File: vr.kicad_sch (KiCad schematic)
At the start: 28 parts, among them U2 ST1PS02CQTR, U3 ST1PS02CQTR, U303 LDLN025M12R, U304 LM2664M6_NOPB

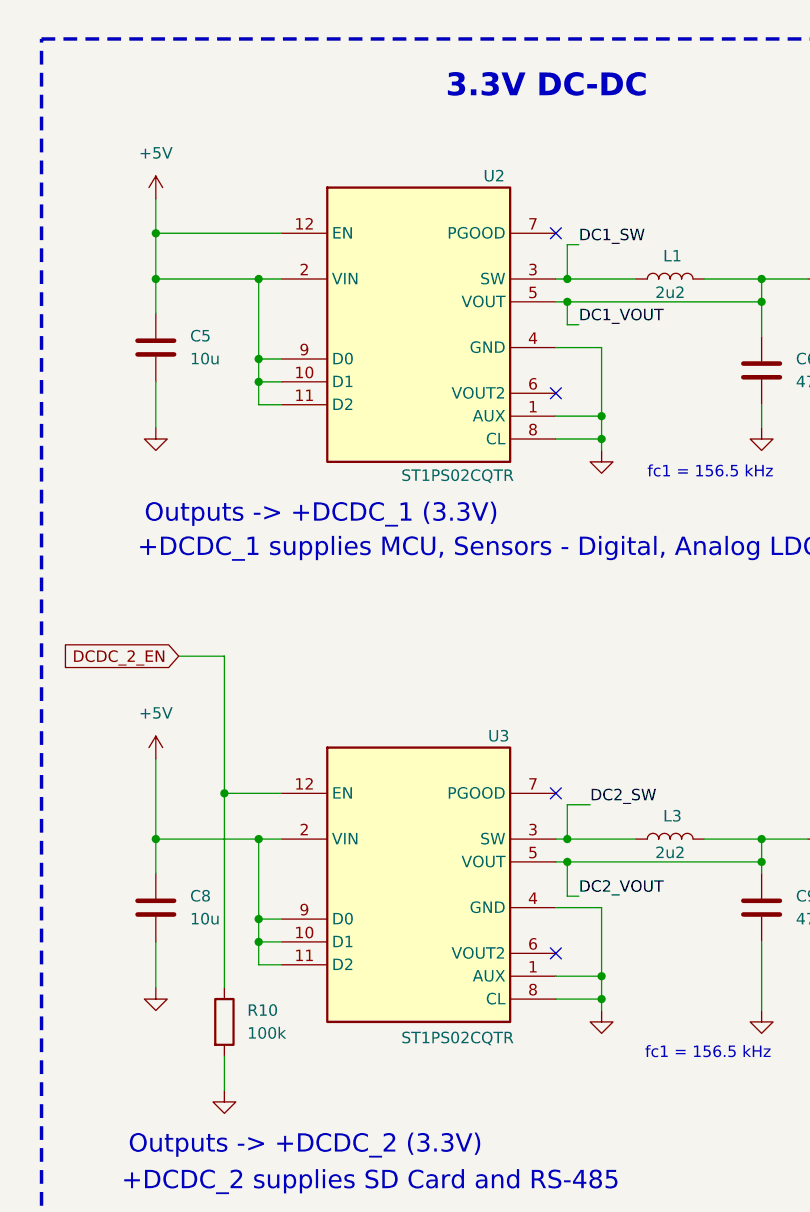
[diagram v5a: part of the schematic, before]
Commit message: schematics errors fixed and ready for PCB
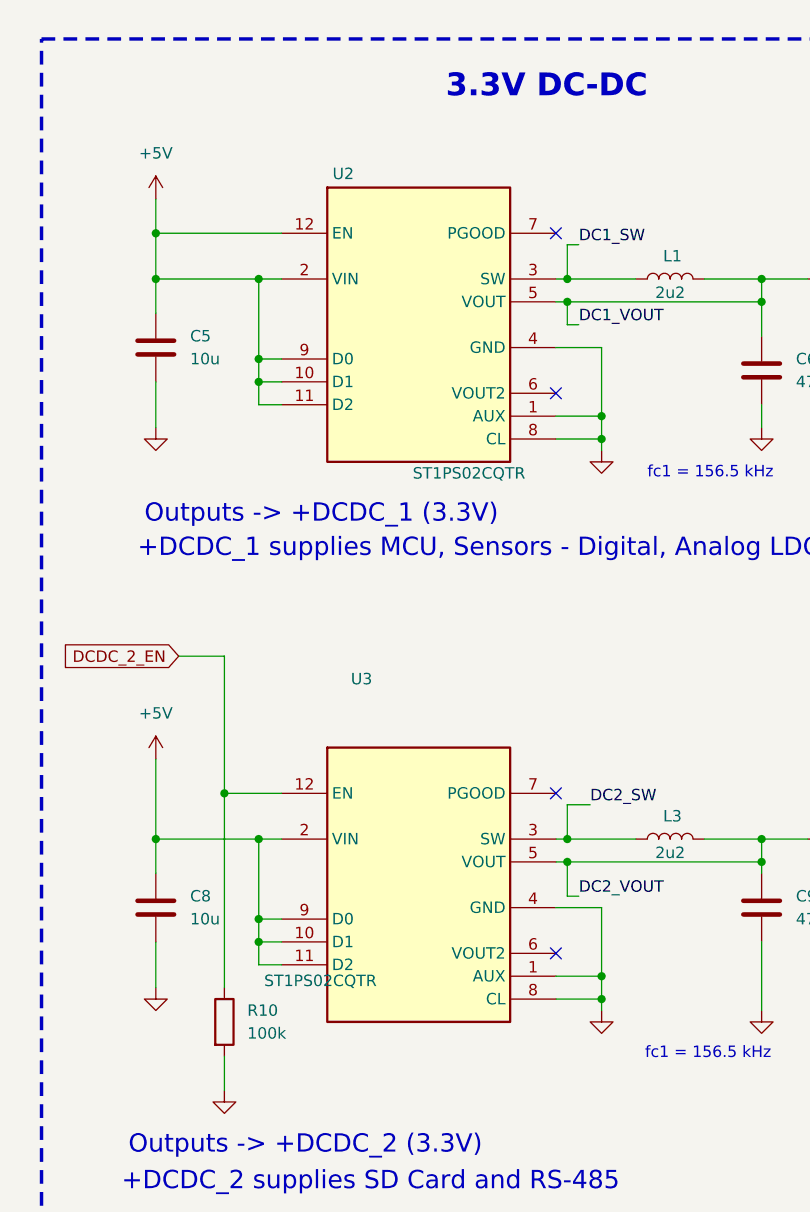
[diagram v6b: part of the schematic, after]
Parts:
- TP2, TP3, TP302, TP304: Distributor_Link https://www.mouser.com/ProductDetail/Keystone-Electronics/5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 -> (none); Manufacturer_Name Keystone Electronics -> (none); Manufacturer_Part_Number 5000 -> (none)
- U2, U3: footprint EMS:ST1PS02CQTR -> QFN40P170X200X55-12N-D; symbol AMS-CM:ST1PS02CQTR -> EMS:ST1PS02CQTR
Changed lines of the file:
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@@
 			)
 		)
-		(property "Datasheet" "https://www.mouser.com/datasheet/2/215/000-5004-741320.pdf"
+		(property "Datasheet" "~"
 			(at 80.01 189.23 0)
 			(effects
@@
 			)
 		)
-		(property "Distributor_Link" "https://www.mouser.com/ProductDetail/Keystone-Electronics/5000?qs=q0tsjPZWdm%252B9SiiTAbEwUw%3D%3D"
+		(property "Distributor_Link" "~"
 			(at 80.01 194.31 0)
 			(effects
@@
 			)
 		)
-		(property "Manufacturer_Name" "Keystone Electronics"
+		(property "Manufacturer_Name" "~"
 			(at 80.01 194.31 0)
 			(effects
@@
 			)
 		)
-		(property "Manufacturer_Part_Number" "5000"
+		(property "Manufacturer_Part_Number" "~"
 			(at 80.01 194.31 0)
 			(effects
@@
 			)
 		)
-		(property "Datasheet" "https://www.mouser.com/datasheet/2/215/000-5004-741320.pdf"
+		(property "Datasheet" "~"
 			(at 43.18 189.23 0)
 			(effects
@@
 			)
 		)
-		(property "Distributor_Link" "https://www.mouser.com/ProductDetail/Keystone-Electronics/5000?qs=q0tsjPZWdm%252B9SiiTAbEwUw%3D%3D"
+		(property "Distributor_Link" "~"
 			(at 43.18 194.31 0)
 			(effects
@@
 			)
 		)
-		(property "Manufacturer_Name" "Keystone Electronics"
+		(property "Manufacturer_Name" "~"
 			(at 43.18 194.31 0)
 			(effects
@@
 			)
 		)
-		(property "Manufacturer_Part_Number" "5000"
+		(property "Manufacturer_Part_Number" "~"
 			(at 43.18 194.31 0)
 			(effects
@@
 			)
 		)
-		(property "Datasheet" "https://www.mouser.com/datasheet/2/215/000-5004-741320.pdf"
+		(property "Datasheet" "~"
 			(at 62.23 189.23 0)
 			(effects
@@
 			)
 		)
-		(property "Distributor_Link" "https://www.mouser.com/ProductDetail/Keystone-Electronics/5000?qs=q0tsjPZWdm%252B9SiiTAbEwUw%3D%3D"
+		(property "Distributor_Link" "~"
 			(at 62.23 194.31 0)
 			(effects
@@
 			)
 		)
-		(property "Manufacturer_Name" "Keystone Electronics"
+		(property "Manufacturer_Name" "~"
 			(at 62.23 194.31 0)
 			(effects
@@
 			)
 		)
-		(property "Manufacturer_Part_Number" "5000"
+		(property "Manufacturer_Part_Number" "~"
 			(at 62.23 194.31 0)
 			(effects
@@
 			)
 		)
-		(property "Datasheet" "https://www.mouser.com/datasheet/2/215/000-5004-741320.pdf"
+		(property "Datasheet" "~"
 			(at 24.13 189.23 0)
 			(effects
@@
 			)
 		)
-		(property "Distributor_Link" "https://www.mouser.com/ProductDetail/Keystone-Electronics/5000?qs=q0tsjPZWdm%252B9SiiTAbEwUw%3D%3D"
+		(property "Distributor_Link" "~"
 			(at 24.13 194.31 0)
 			(effects
@@
 			)
 		)
-		(property "Manufacturer_Name" "Keystone Electronics"
+		(property "Manufacturer_Name" "~"
 			(at 24.13 194.31 0)
 			(effects
@@
 			)
 		)
-		(property "Manufacturer_Part_Number" "5000"
+		(property "Manufacturer_Part_Number" "~"
 			(at 24.13 194.31 0)
 			(effects
@@
 	)
 	(symbol
-		(lib_id "AMS-CM:ST1PS02CQTR")
-		(at 57.15 123.19 0)
+		(lib_id "EMS:ST1PS02CQTR")
+		(at 41.91 116.84 0)
 		(unit 1)
 		(exclude_from_sim no)
@@
 		(dnp no)
 		(property "Reference" "U3"
-			(at 66.04 107.95 0)
+			(at 50.8 101.6 0)
 			(effects
 				(font
@@
 		)
 		(property "Value" "ST1PS02CQTR"
-			(at 61.468 141.478 0)
+			(at 46.228 135.128 0)
 			(effects
 				(font
@@
 			)
 		)
-		(property "Footprint" "EMS:ST1PS02CQTR"
+		(property "Footprint" "QFN40P170X200X55-12N-D"
 			(at 43.434 148.59 0)
 			(effects
@@
 		)
 		(property "Height" "0.55"
-			(at 83.82 513.03 0)
+			(at 68.58 506.68 0)
 			(effects
 				(font
@@
 		)
 		(property "Mouser Part Number" "511-ST1PS02CQTR"
-			(at 83.82 613.03 0)
+			(at 68.58 606.68 0)
 			(effects
 				(font
@@
 		)
 		(property "Mouser Price/Stock" "https://www.mouser.co.uk/ProductDetail/STMicroelectronics/ST1PS02CQTR?qs=sPbYRqrBIVkrGj42PMRzhg%3D%3D"
-			(at 83.82 713.03 0)
+			(at 68.58 706.68 0)
 			(effects
 				(font
@@
 		)
 		(property "Manufacturer_Name" "STMicroelectronics"
-			(at 83.82 813.03 0)
+			(at 68.58 806.68 0)
 			(effects
 				(font
@@
 		)
 		(property "Manufacturer_Part_Number" "ST1PS02CQTR"
-			(at 83.82 913.03 0)
+			(at 68.58 906.68 0)
 			(effects
 				(font
@@
 		)
 		(property "Arrow Part Number" ""
-			(at 57.15 123.19 0)
+			(at 41.91 116.84 0)
 			(effects
 				(font
@@
 		)
 		(property "Arrow Price/Stock" ""
-			(at 57.15 123.19 0)
+			(at 41.91 116.84 0)
 			(effects
 				(font
@@
 		)
 		(property "Distributor_Link" "https://www.mouser.co.uk/ProductDetail/STMicroelectronics/ST1PS02CQTR?qs=sPbYRqrBIVkrGj42PMRzhg%3D%3D"
-			(at 57.15 123.19 0)
+			(at 41.91 116.84 0)
 			(effects
 				(font
@@
 	)
 	(symbol
-		(lib_id "AMS-CM:ST1PS02CQTR")
-		(at 57.15 60.96 0)
+		(lib_id "EMS:ST1PS02CQTR")
+		(at 41.91 54.61 0)
 		(unit 1)
 		(exclude_from_sim no)
@@
 		(dnp no)
 		(property "Reference" "U2"
-			(at 65.532 45.72 0)
+			(at 48.768 45.466 0)
 			(effects
 				(font
@@
 		)
 		(property "Value" "ST1PS02CQTR"
-			(at 61.468 78.994 0)
+			(at 62.738 78.74 0)
 			(effects
 				(font
@@
 			)
 		)
-		(property "Footprint" "EMS:ST1PS02CQTR"
+		(property "Footprint" "QFN40P170X200X55-12N-D"
 			(at 43.434 86.36 0)
 			(effects
@@
 		)
 		(property "Height" "0.55"
-			(at 83.82 450.8 0)
+			(at 68.58 444.45 0)
 			(effects
 				(font
@@
 		)
 		(property "Mouser Part Number" "511-ST1PS02CQTR"
-			(at 83.82 550.8 0)
+			(at 68.58 544.45 0)
 			(effects
 				(font
@@
 		)
 		(property "Mouser Price/Stock" "https://www.mouser.co.uk/ProductDetail/STMicroelectronics/ST1PS02CQTR?qs=sPbYRqrBIVkrGj42PMRzhg%3D%3D"
-			(at 83.82 650.8 0)
+			(at 68.58 644.45 0)
 			(effects
 				(font
@@
 		)
 		(property "Manufacturer_Name" "STMicroelectronics"
-			(at 83.82 750.8 0)
+			(at 68.58 744.45 0)
 			(effects
 				(font
@@
 		)
 		(property "Manufacturer_Part_Number" "ST1PS02CQTR"
-			(at 83.82 850.8 0)
+			(at 68.58 844.45 0)
 			(effects
 				(font
@@
 		)
 		(property "Arrow Part Number" ""
-			(at 57.15 60.96 0)
+			(at 41.91 54.61 0)
 			(effects
 				(font
@@
 		)
 		(property "Arrow Price/Stock" ""
-			(at 57.15 60.96 0)
+			(at 41.91 54.61 0)
 			(effects
 				(font
@@
 		)
 		(property "Distributor_Link" "https://www.mouser.co.uk/ProductDetail/STMicroelectronics/ST1PS02CQTR?qs=sPbYRqrBIVkrGj42PMRzhg%3D%3D"
-			(at 57.15 60.96 0)
+			(at 41.91 54.61 0)
 			(effects
 				(font

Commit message: new version created. Now at v2.0.0
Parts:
- U2, U3: footprint QFN40P170X200X55-12N-D -> EMS:ST1PS02CQTR
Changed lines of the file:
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@@
 			)
 		)
-		(property "Footprint" "QFN40P170X200X55-12N-D"
+		(property "Footprint" "EMS:ST1PS02CQTR"
 			(at 43.434 148.59 0)
 			(effects
@@
 			)
 		)
-		(property "Footprint" "QFN40P170X200X55-12N-D"
+		(property "Footprint" "EMS:ST1PS02CQTR"
 			(at 43.434 86.36 0)
 			(effects
